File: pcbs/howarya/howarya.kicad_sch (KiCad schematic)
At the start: 64 parts, among them J1 TRRS, SW1 MX, SW10 MX, SW11 MX, SW12 MX, SW13 MX, SW14 MX, SW15 MX, SW16 MX, SW17 MX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

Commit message: Name change
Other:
- title: Swoop MX -> Howarya?
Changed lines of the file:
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@@
   (paper "A4")
   (title_block
-    (title "Swoop MX")
-    (date "2021-12-11")
-    (rev "0.1")
+    (title "Howarya?")
+    (date "2022-02-03")
+    (rev "0.2.1")
     (company "jmnw")
   )

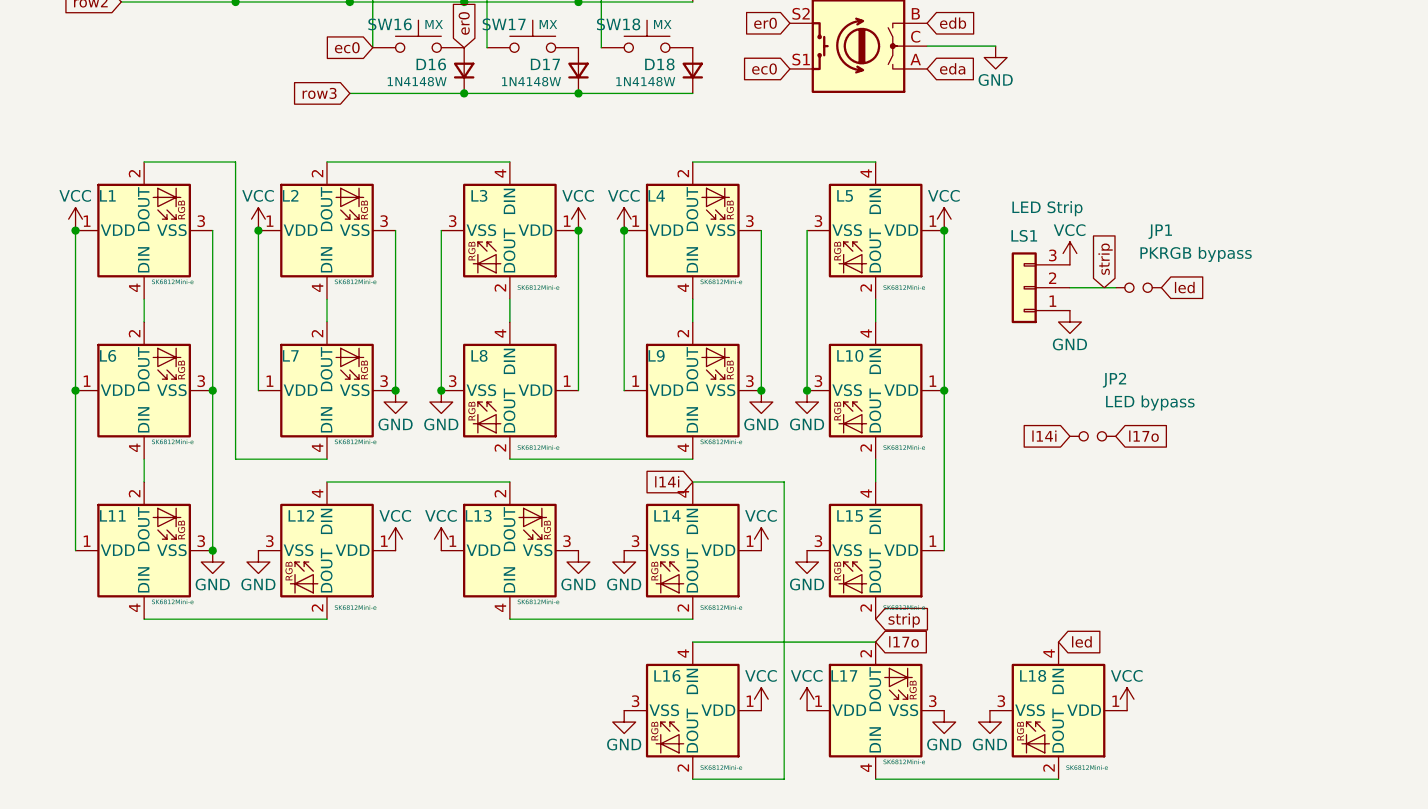
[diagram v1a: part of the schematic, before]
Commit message: Removed LED strip and normalised LED order.
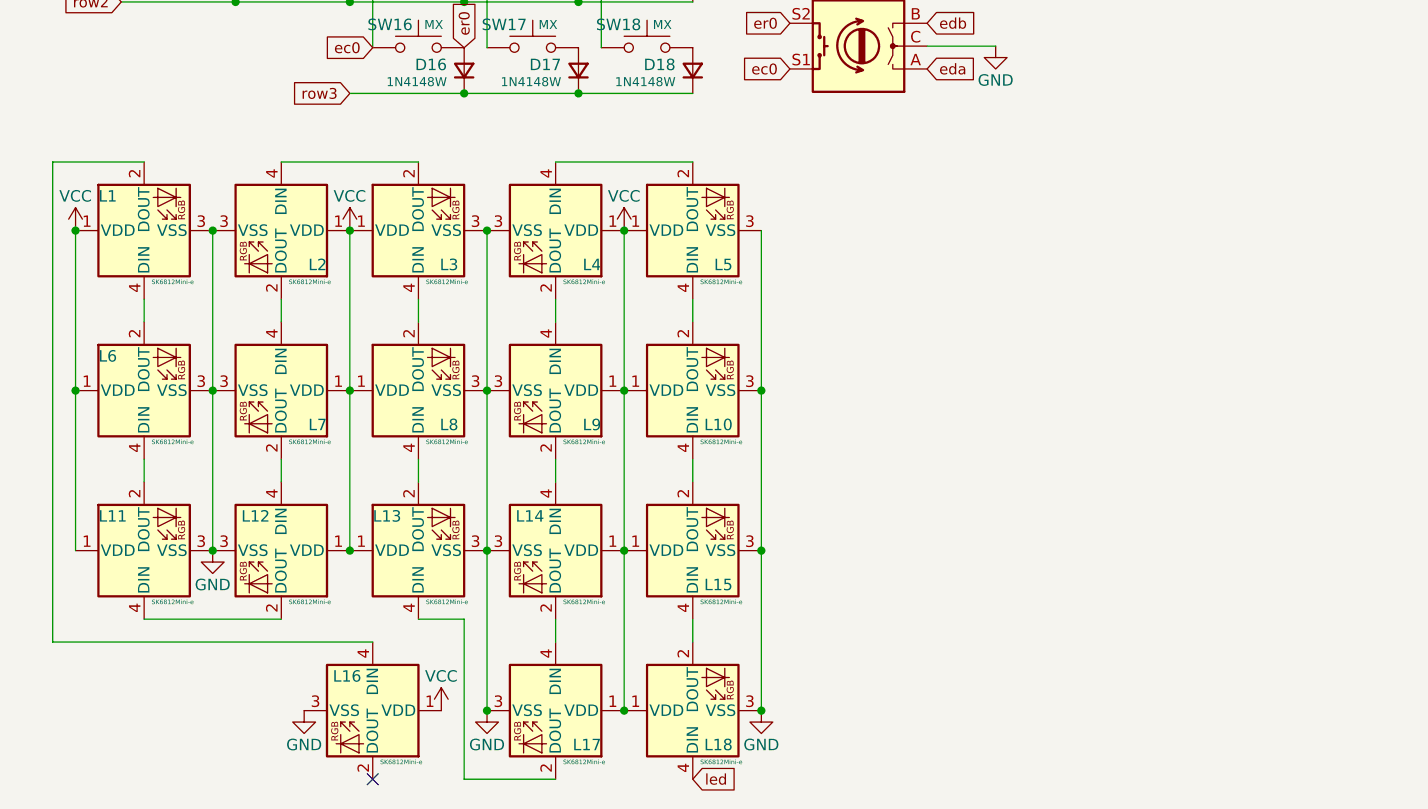
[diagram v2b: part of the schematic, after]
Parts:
- removed JP1: PKRGB bypass, swoop:Jumper, symbol Device:Jumper_NO_Small
- removed JP2: LED bypass, swoop:Jumper, symbol Device:Jumper_NO_Small
- removed LS1: LED Strip, swoop:StripLED, symbol Connector_Generic:Conn_01x03
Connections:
- net strip is gone; now on an unnamed net: L15.2 (DOUT)
- net at L10.2 (DOUT): now also L5.4 (DIN); no longer L15.4 (DIN)
- net at L10.4 (DIN): no longer L5.2 (DOUT)
- net at L17.4 (DIN): now also L14.2 (DOUT); no longer L18.2 (DOUT)
- net at L3.2 (DOUT): now also L2.4 (DIN); no longer L8.4 (DIN)
- net at L3.4 (DIN): now also L8.2 (DOUT); no longer L2.2 (DOUT)
- net at L4.2 (DOUT): now also L9.4 (DIN); no longer L5.4 (DIN)
- net at L7.2 (DOUT): now also L12.4 (DIN); no longer L2.4 (DIN)
- net at L4.4 (DIN): now also L5.2 (DOUT); no longer L9.2 (DOUT)
- net at L13.2 (DOUT): now also L8.4 (DIN); no longer L12.4 (DIN)
- net at L13.4 (DIN): now also L17.2 (DOUT); no longer L14.2 (DOUT)
- net at L7.4 (DIN): now also L2.2 (DOUT); no longer L1.2 (DOUT)
- net l14i: no longer names the net of L14.4 (DIN)
- net l14i: now also L9.2 (DOUT); no longer L16.2 (DOUT)
- net l17o: no longer names the net of L16.4 (DIN)
- net l17o: now also L1.2 (DOUT); no longer L17.2 (DOUT)
- new net: L15.4 (DIN), L18.2 (DOUT)
- no-connect marks 4 -> 5
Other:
- moved on the sheet: L10, L12, L13, L14, L15, L16, L17, L18, L2, L3, L4, L5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
